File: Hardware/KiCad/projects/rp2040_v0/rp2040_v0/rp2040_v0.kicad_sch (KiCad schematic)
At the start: 57 parts, among them J1 Conn_01x03, J11 Conn_01x02, J12 Screw_Terminal_01x02, J2 Conn_01x02, J3 Conn_01x03, J4 Conn_01x04, J5 USB_B_Micro, J6 Conn_01x02, J7 Conn_01x02, J8 Conn_01x03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

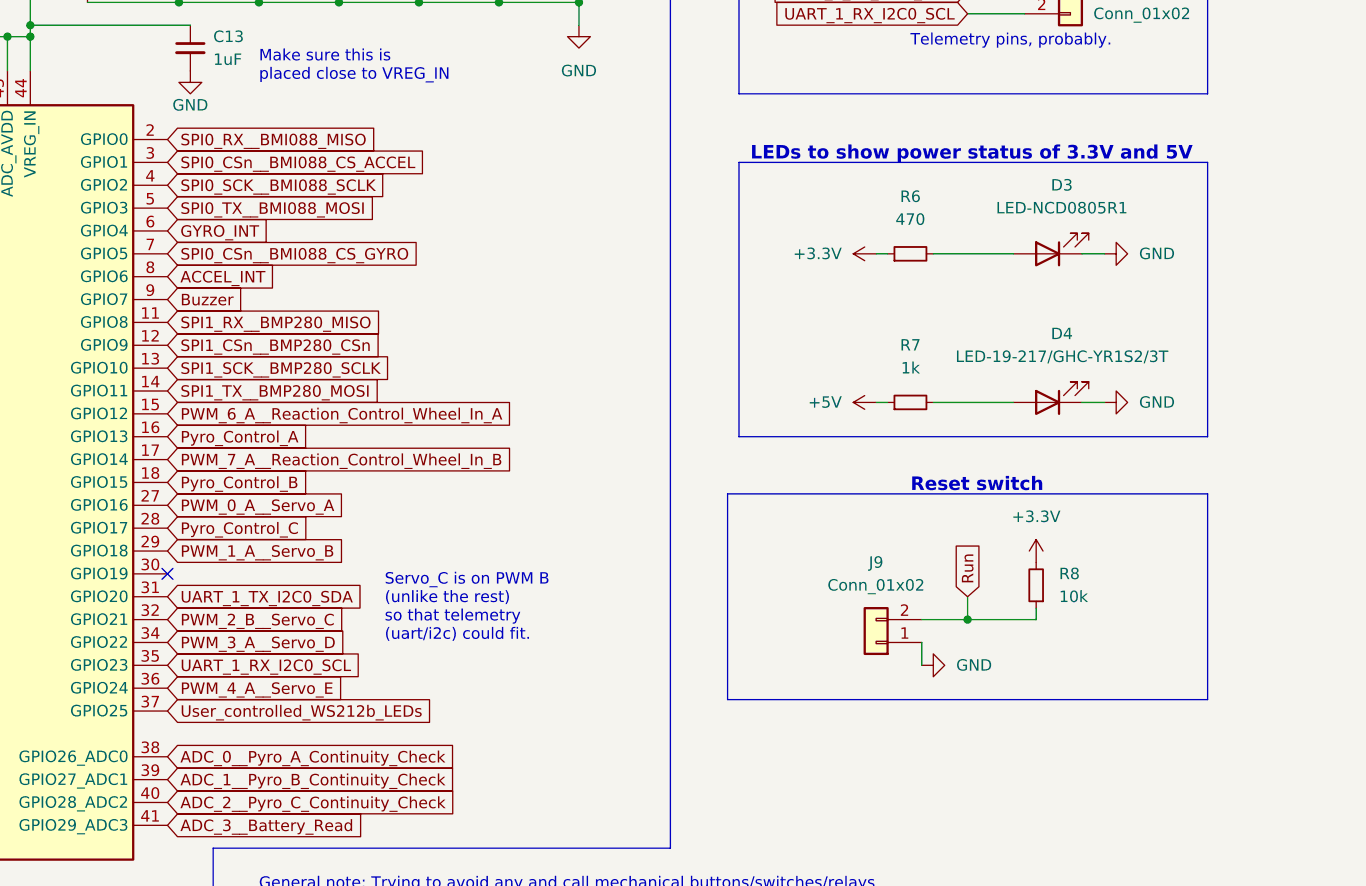
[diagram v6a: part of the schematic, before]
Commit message: Swap out ws2812b led for small red and green led.
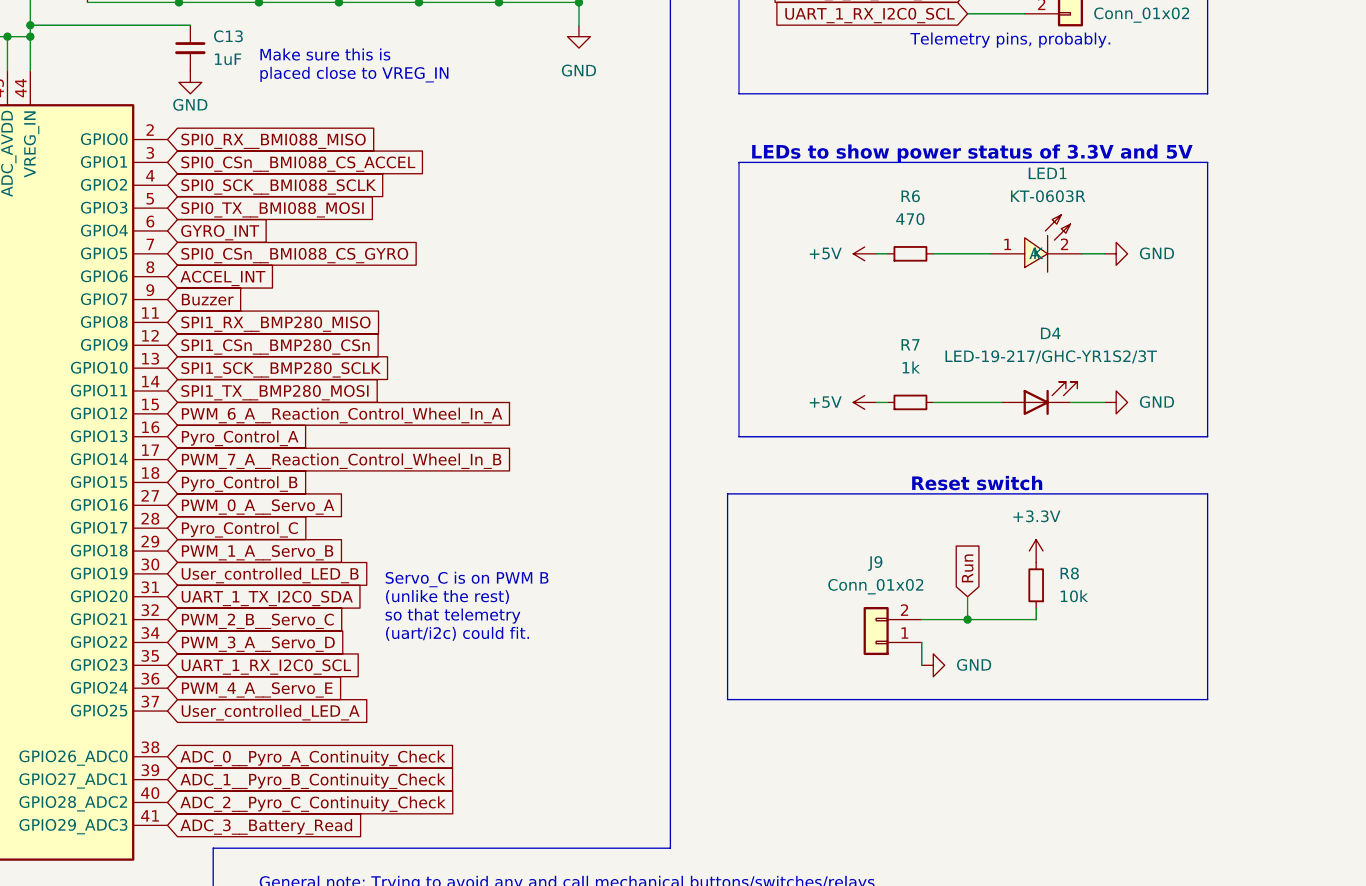
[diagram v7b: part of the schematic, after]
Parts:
- removed D3: LED-NCD0805R1, easyeda2kicad:LED0805-RD, symbol Device:LED
- added LED1: KT-0603R, easyeda2kicad:LED0603-R-RD, symbol easyeda2kicad_flight_computer:KT-0603R
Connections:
- net +3.3V: no longer R6.1
- net +5V: now also R6.1
- net -BATT: now also LED1.2 (K)
- net at R6.2: now also LED1.1 (A)
- net User_controlled_LED_B: now reaches U3.30 (GPIO19)
- net User_controlled_WS212b_LEDs renamed User_controlled_LED_A
- no-connect marks 3 -> 2
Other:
- moved on the sheet: D4

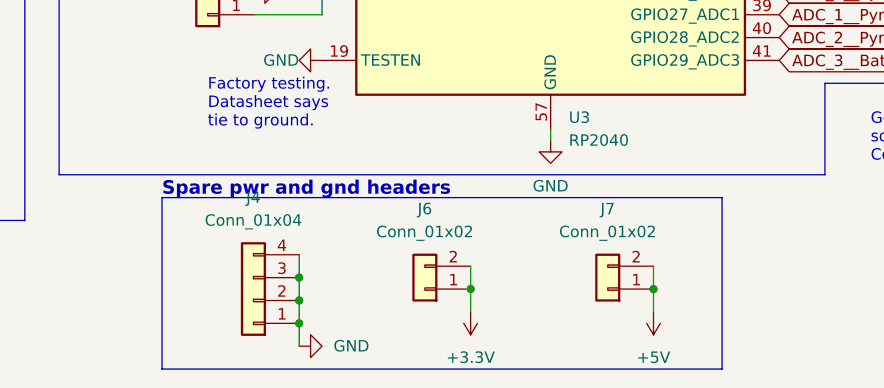
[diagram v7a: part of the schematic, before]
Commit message: Make mounting holes smaller. Remove and combine extra power headers
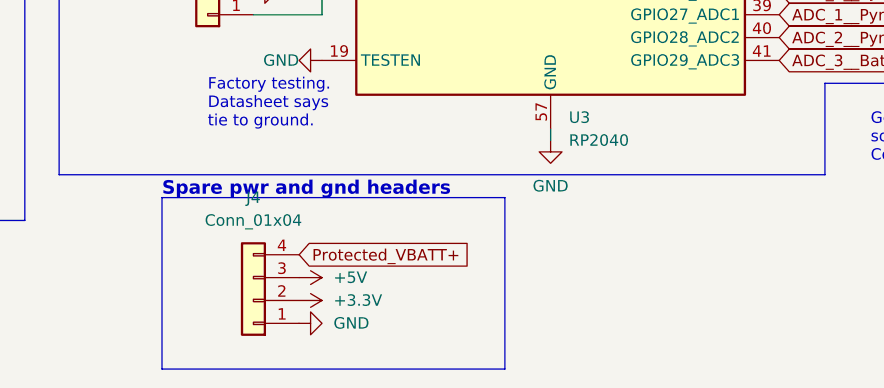
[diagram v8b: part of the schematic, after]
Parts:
- removed J6, J7: Conn_01x02, Connector_PinHeader_2.54mm:PinHeader_1x02_P2.54mm_Vertical, symbol Connector_Generic:Conn_01x02
- H1, H2, H3, H4: footprint MountingHole:MountingHole_3.2mm_M3 -> MountingHole:MountingHole_2mm
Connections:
- net +3.3V: now also J4.2 (Pin_2)
- net +5V: now also J4.3 (Pin_3)
- net -BATT: no longer J4.2 (Pin_2), J4.3 (Pin_3), J4.4 (Pin_4)
- net Protected_VBATT+: now also J4.4 (Pin_4)
